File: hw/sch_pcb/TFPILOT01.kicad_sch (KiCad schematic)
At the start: 80 parts, among them IC1 MIMXRT1062DVJ6B, J1 Conn_01x11_Male, J2 Conn_01x11_Male, J3 Conn_01x12_Male, J4 Conn_01x11_Male, J5 Conn_01x11_Male, J6 Conn_01x03_Male, J7 Conn_01x03_Male, P2 D26, Q1 Q_PMOS_GDS_DMP3125L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

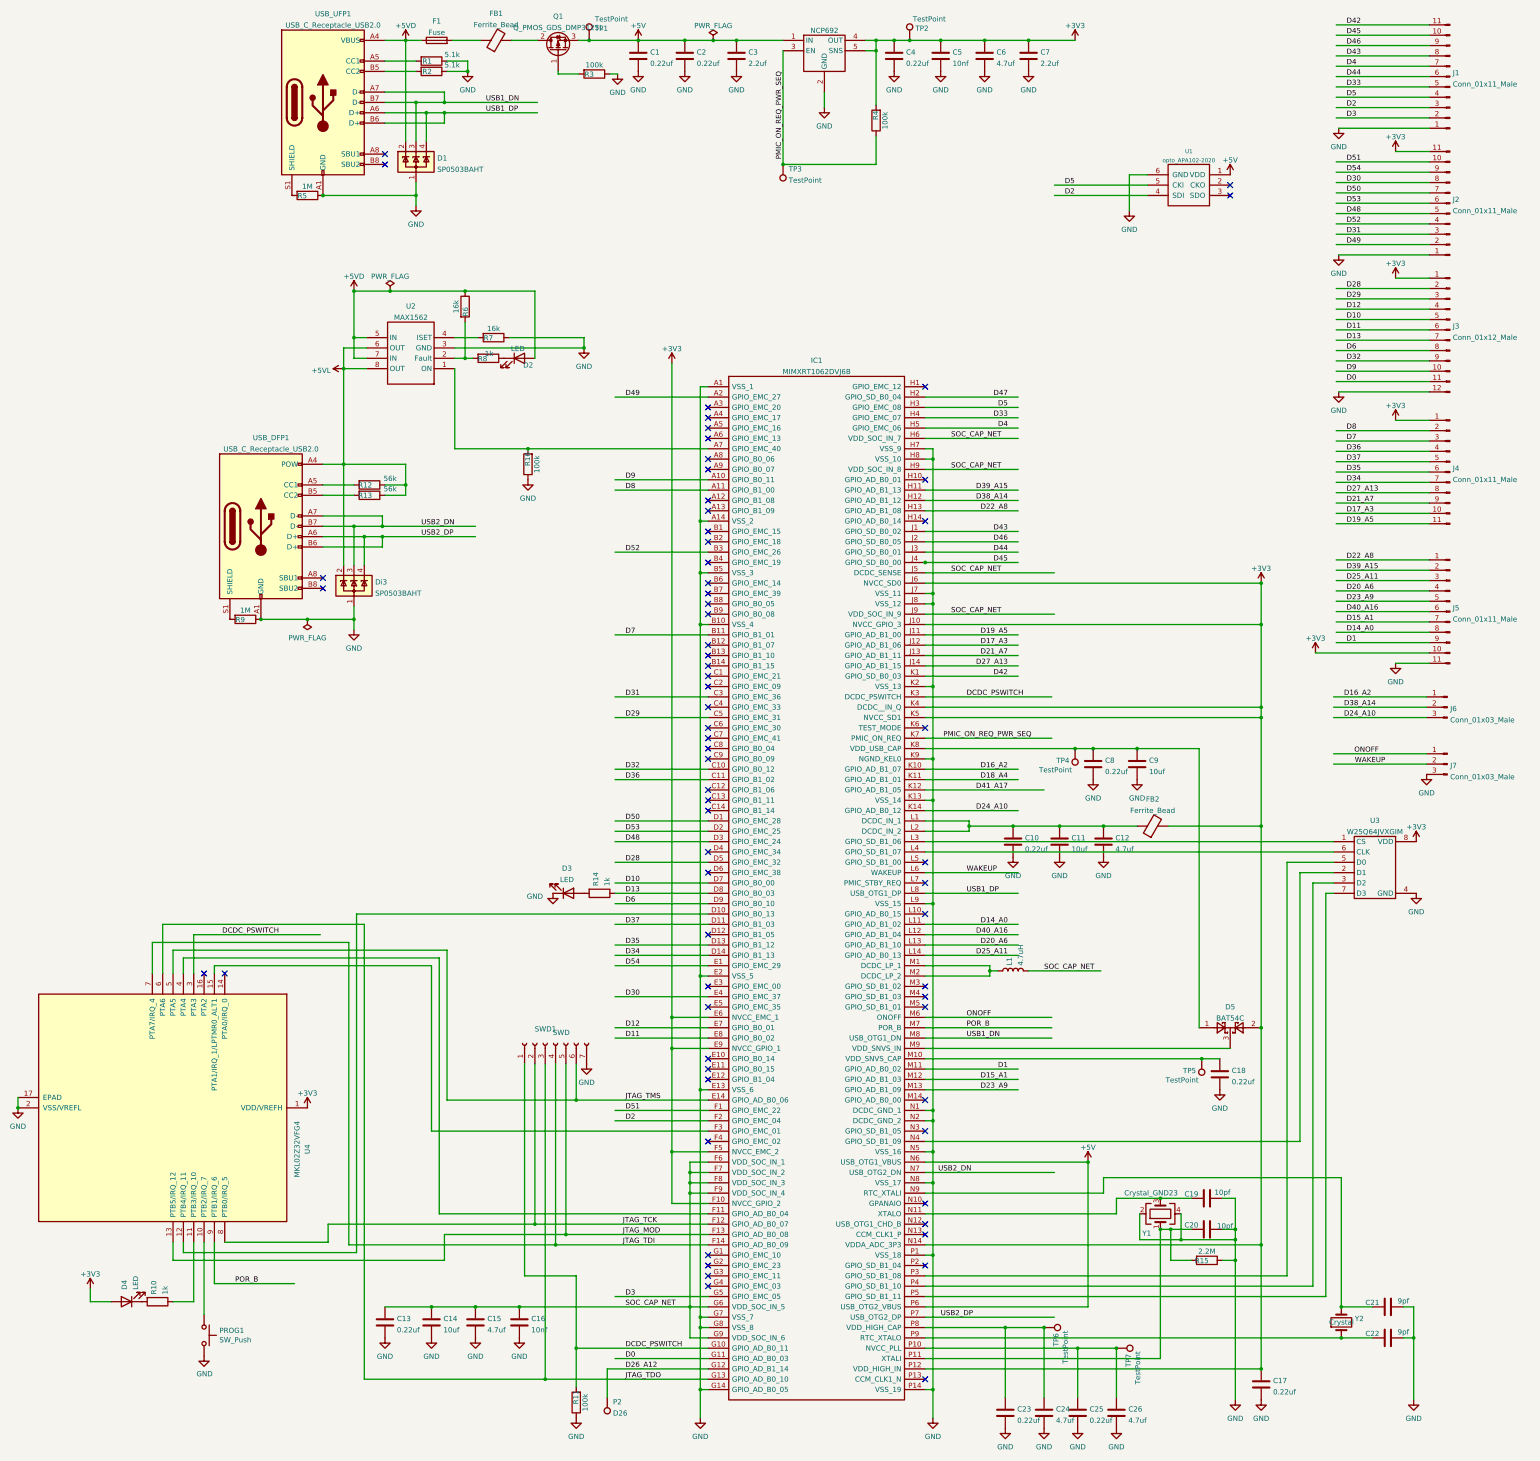
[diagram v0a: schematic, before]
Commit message: Remove USB-C host connector.
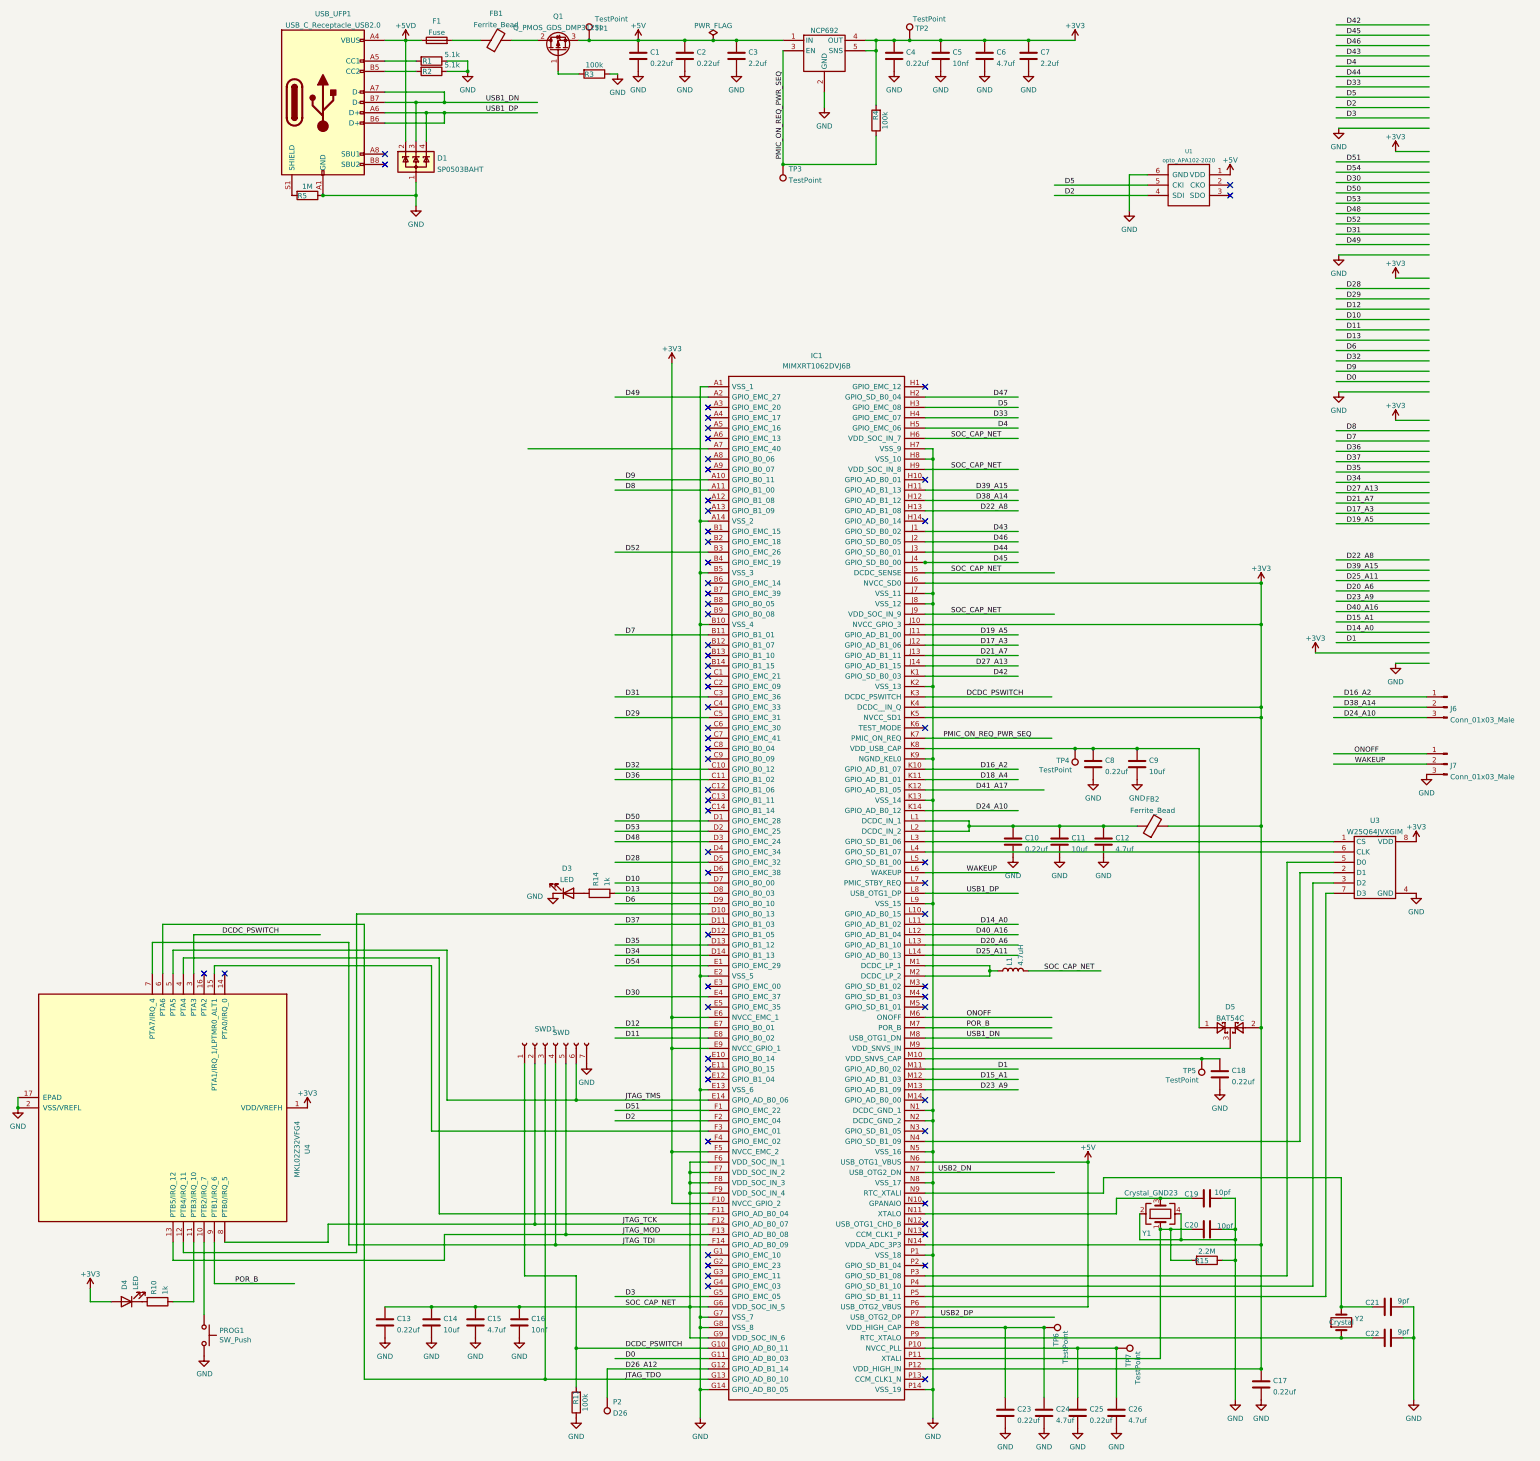
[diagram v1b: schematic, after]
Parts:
- removed D2: LED, LED_SMD:LED_0402_1005Metric, symbol Device:LED
- removed Di3: SP0503BAHT, Package_TO_SOT_SMD:SOT-143, symbol Power_Protection:SP0503BAHT
- removed J1, J2, J4, J5: Conn_01x11_Male, Connector_PinHeader_2.54mm:PinHeader_1x11_P2.54mm_Vertical, symbol Connector:Conn_01x11_Male
- removed J3: Conn_01x12_Male, Connector_PinHeader_2.54mm:PinHeader_1x12_P2.54mm_Vertical, symbol Connector:Conn_01x12_Male
- removed R12, R13: 56k, Resistor_SMD:R_0603_1608Metric, symbol Device:R
- removed R16: 100k, Resistor_SMD:R_0603_1608Metric, symbol Device:R
- removed R6, R7: 16k, Resistor_SMD:R_0603_1608Metric, symbol Device:R
- removed R8: 1k, Resistor_SMD:R_0402_1005Metric, symbol Device:R
- removed R9: 1M, Resistor_SMD:R_0603_1608Metric, symbol Device:R
- removed U2: MAX1562, Package_SO:SO-8_3.9x4.9mm_P1.27mm, symbol MIMXRT1062DVJ6B:MAX1562
- removed USB_DFP1: USB_C_Receptacle_USB2.0, USB-C-Power-tester:TYPE-C-31-M-14, symbol simonsen:USB_C_Receptacle_USB2.0_NOPOW
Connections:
- no-connect marks 66 -> 64
